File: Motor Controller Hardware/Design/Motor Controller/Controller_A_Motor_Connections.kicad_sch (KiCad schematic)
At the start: 26 parts, among them J4 Screw_Terminal_01x03, J5 Screw_Terminal_01x02, J6 Screw_Terminal_01x06, J9 Screw_Terminal_01x03, U12 74LVC3G17, U13 74LVC3G17

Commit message: Almost done power delivery
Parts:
- renumbered C79 to C100, C75 to C93, C76 to C94, C80 to C95, C77 to C96, C81 to C97, C78 to C98, C82 to C99, J5 to J14, J6 to J15, J4 to J16, J9 to J17, R31 to R50, R17 to R51, R32 to R52, R28 to R53, R33 to R54, R18 to R55, R34 to R56, R29 to R57, R35 to R58, R27 to R59, R36 to R60, R30 to R61, U12 to U15, U13 to U16

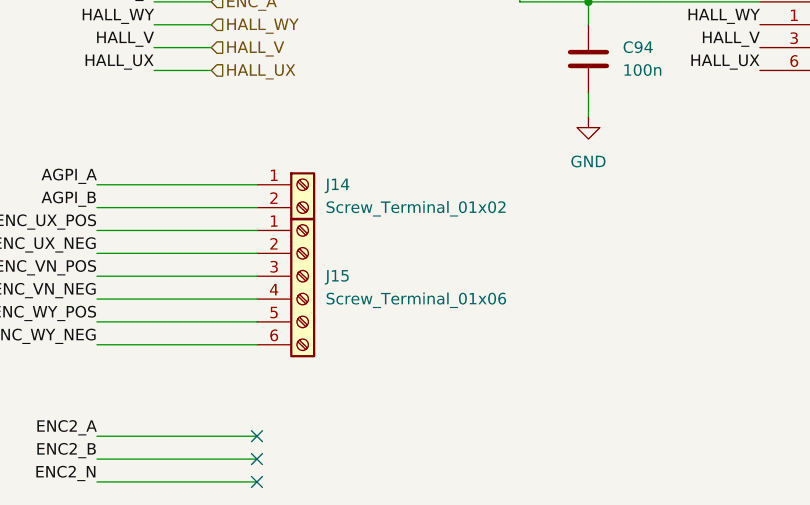
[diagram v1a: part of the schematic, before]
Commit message: Added foot prints and started layout
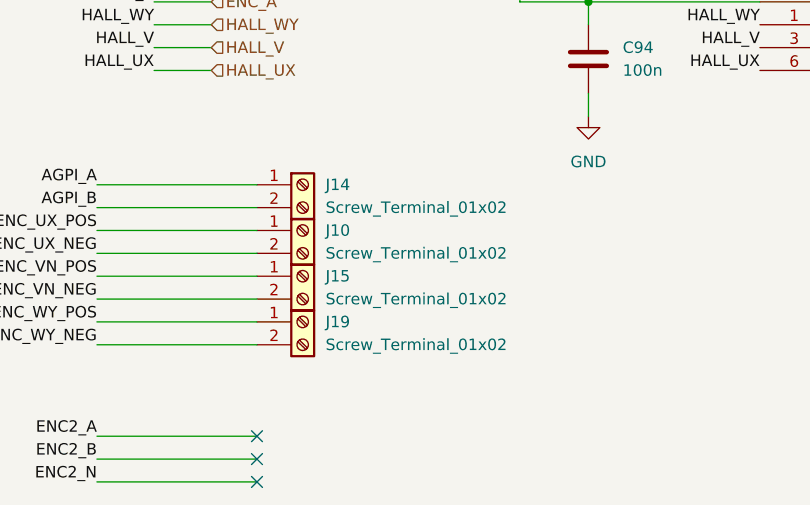
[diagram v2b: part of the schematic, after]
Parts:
- removed J15: Screw_Terminal_01x06, symbol Connector:Screw_Terminal_01x06
- added J10, J15, J19: Screw_Terminal_01x02, TerminalBlock_Phoenix:TerminalBlock_Phoenix_MPT-0,5-2-2.54_1x02_P2.54mm_Horizontal, symbol Connector:Screw_Terminal_01x02
- C100, C93, C94, C95, C96, C97, C98, C99: footprint (none) -> Capacitor_SMD:C_0603_1608Metric
- J14, J16, J17: footprint (none) -> TerminalBlock_Phoenix:TerminalBlock_Phoenix_MPT-0,5-2-2.54_1x02_P2.54mm_Horizontal
- R50, R51, R52, R53, R54, R55, R56, R57, R58, R59, R60, R61: footprint (none) -> Resistor_SMD:R_0603_1608Metric
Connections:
- net AENC_UX_NEG: now also J10.2 (Pin_2)
- net AENC_UX_POS: now also J10.1 (Pin_1)
- net AENC_VN_NEG: now also J15.2 (Pin_2)
- net AENC_VN_POS: now also J15.1 (Pin_1)
- net AENC_WY_NEG: now also J19.2 (Pin_2)
- net AENC_WY_POS: now also J19.1 (Pin_1)

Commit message: A
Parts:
- J16, J17: footprint TerminalBlock_Phoenix:TerminalBlock_Phoenix_MPT-0,5-2-2.54_1x02_P2.54mm_Horizontal -> TerminalBlock_Phoenix:TerminalBlock_Phoenix_MPT-0,5-3-2.54_1x03_P2.54mm_Horizontal
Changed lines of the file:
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@@
 			)
 		)
-		(property "Footprint" "TerminalBlock_Phoenix:TerminalBlock_Phoenix_MPT-0,5-2-2.54_1x02_P2.54mm_Horizontal"
+		(property "Footprint" "TerminalBlock_Phoenix:TerminalBlock_Phoenix_MPT-0,5-3-2.54_1x03_P2.54mm_Horizontal"
 			(at 238.76 111.76 0)
 			(effects
@@
 			)
 		)
-		(property "Footprint" "TerminalBlock_Phoenix:TerminalBlock_Phoenix_MPT-0,5-2-2.54_1x02_P2.54mm_Horizontal"
+		(property "Footprint" "TerminalBlock_Phoenix:TerminalBlock_Phoenix_MPT-0,5-3-2.54_1x03_P2.54mm_Horizontal"
 			(at 238.76 60.96 0)
 			(effects

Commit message: Will now just do rev 1 as Silicon mosfets and rev 2 will be gan
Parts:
- U15, U16: footprint https://assets.nexperia.com/documents/data-sheet/74LVC3G17.pdf -> Package_SO:TSSOP-8_3x3mm_P0.65mm; DK# (none) -> 1727-5998-1-ND
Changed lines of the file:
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@@
 			)
 		)
-		(property "Footprint" "https://assets.nexperia.com/documents/data-sheet/74LVC3G17.pdf"
+		(property "Footprint" "Package_SO:TSSOP-8_3x3mm_P0.65mm"
 			(at 143.51 110.49 0)
 			(effects
@@
 			)
 		)
-		(property "Datasheet" ""
+		(property "Datasheet" "https://assets.nexperia.com/documents/data-sheet/74LVC3G17.pdf"
 			(at 143.51 110.49 0)
 			(effects
@@
 			)
 		)
+		(property "DK#" "1727-5998-1-ND"
+			(at 143.51 110.49 0)
+			(effects
+				(font
+					(size 1.27 1.27)
+				)
+				(hide yes)
+			)
+		)
 		(pin "5"
 		)
@@
 			)
 		)
-		(property "Footprint" "https://assets.nexperia.com/documents/data-sheet/74LVC3G17.pdf"
+		(property "Footprint" "Package_SO:TSSOP-8_3x3mm_P0.65mm"
 			(at 143.51 59.69 0)
 			(effects
@@
 			)
 		)
-		(property "Datasheet" ""
+		(property "Datasheet" "https://assets.nexperia.com/documents/data-sheet/74LVC3G17.pdf"
 			(at 143.51 59.69 0)
 			(effects
@@
 			(at 143.51 59.69 0)
 			(effects
+				(font
+					(size 1.27 1.27)
+				)
+				(hide yes)
+			)
+		)
+		(property "DK#" "1727-5998-1-ND"
+			(at 143.51 59.69 0)
+			(effects

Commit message: A
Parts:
- removed C100, C96, C98: 1n, Capacitor_SMD:C_0603_1608Metric, symbol Device:C
- removed C93: 100n, Capacitor_SMD:C_0603_1608Metric, symbol Device:C
- removed J10, J14, J15, J19: Screw_Terminal_01x02, TerminalBlock_Phoenix:TerminalBlock_Phoenix_MPT-0,5-2-2.54_1x02_P2.54mm_Horizontal, symbol Connector:Screw_Terminal_01x02
- removed J16: Screw_Terminal_01x03, TerminalBlock_Phoenix:TerminalBlock_Phoenix_MPT-0,5-3-2.54_1x03_P2.54mm_Horizontal, symbol Connector:Screw_Terminal_01x03
- removed R51, R53, R55, R57, R59, R61: 4k7, Resistor_SMD:R_0603_1608Metric, symbol Device:R
- removed U15: 74LVC3G17, Package_SO:TSSOP-8_3x3mm_P0.65mm, symbol Motor Controller:74LVC3G17
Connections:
- no-connect marks 3 -> 0

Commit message: A
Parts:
- renumbered C94 to C92, C95 to C94, C97 to C95, C99 to C97, J17 to J10, R56 to R55, R58 to R56, R60 to R57, U16 to U14
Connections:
- net HALL_UX renamed HALL_U
- net HALL_WY renamed HALL_W
